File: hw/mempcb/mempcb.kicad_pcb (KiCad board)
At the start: 4 copper layers, 100 x 100 mm, 32 parts, among them J1 RC6502_Bus, J2 0.1" 2x25, U3 JEDEC_DIP32_RAM, U4 74LS138, U5 74LS138

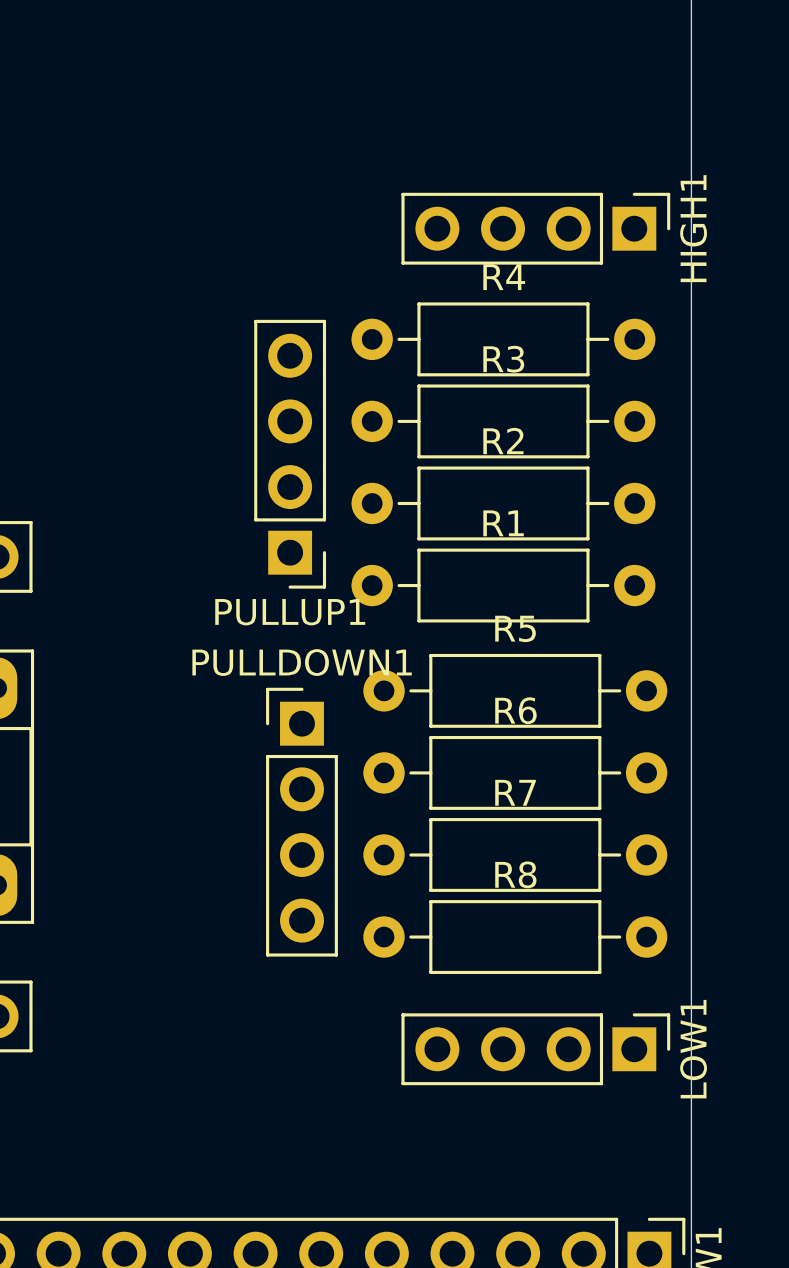
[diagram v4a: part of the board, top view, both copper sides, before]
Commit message: hw/mempcb/: Use just 4 pins instead of 8 for spare GND/Vcc
These don't need to be separate for each circuit, as the pullups do.
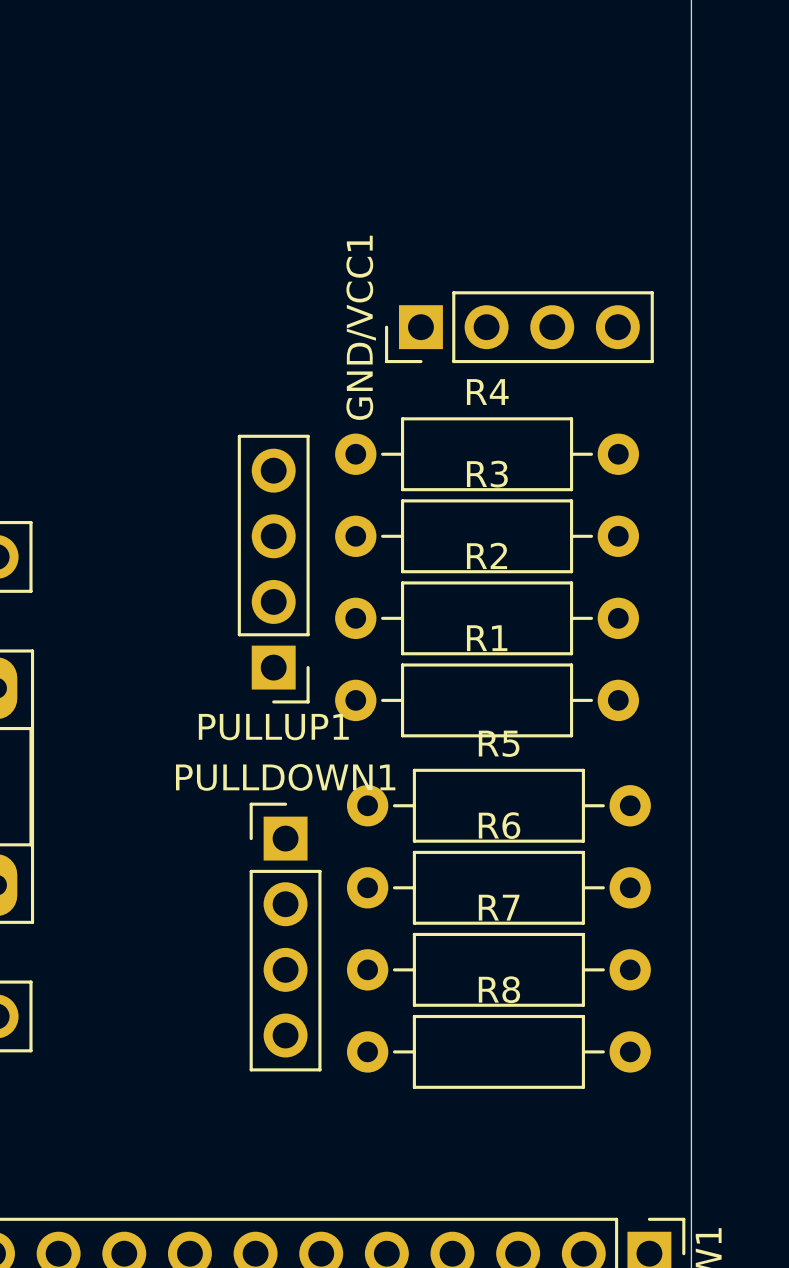
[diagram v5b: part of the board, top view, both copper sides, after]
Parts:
- removed LOW1: 0.1" 1x4, Connector_PinHeader_2.54mm:PinHeader_1x04_P2.54mm_Vertical
- moved GND/VCC1 9.09 mm to (169.5, 108.9), turned to 90 degrees
- moved R7 4.49 mm to (167.5, 133.8)
- moved R5 4.49 mm to (167.5, 127.4)
- moved R4 4.49 mm to (167.0, 113.8)
- moved R6 4.49 mm to (167.5, 130.6)
- moved R8 4.49 mm to (167.5, 137.0)
- moved PULLDOWN1 4.49 mm to (164.3, 128.7)
- moved PULLUP1 4.49 mm to (163.8, 122.1)
- moved R1 4.49 mm to (167.0, 123.4)
- moved R2 4.49 mm to (167.0, 120.2)
- moved R3 4.49 mm to (167.0, 117.0)
- renumbered HIGH1 to GND/VCC1
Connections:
- GND/VCC1 pad 1: /VCC -> /GND
- GND/VCC1 pad 2: /VCC -> /GND

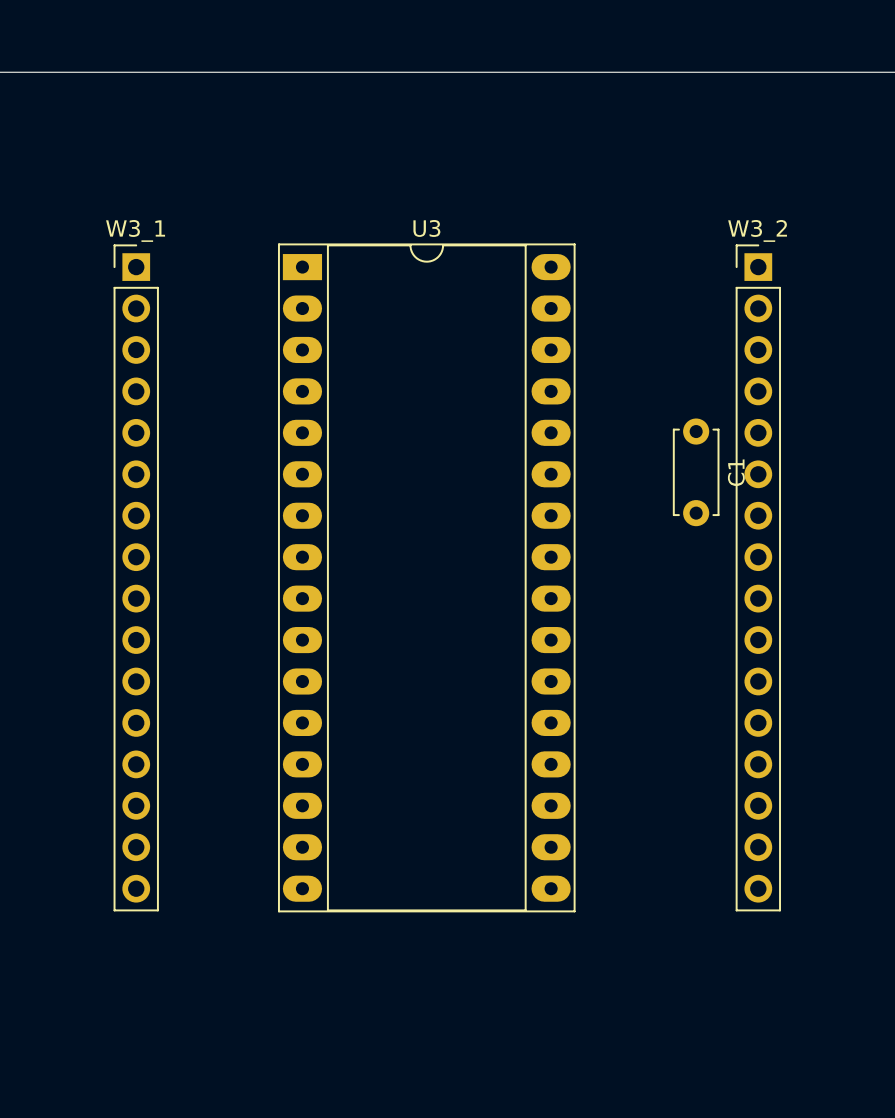
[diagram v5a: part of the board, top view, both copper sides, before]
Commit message: hw/mempcb/: Update ZIF socket footprint in layout
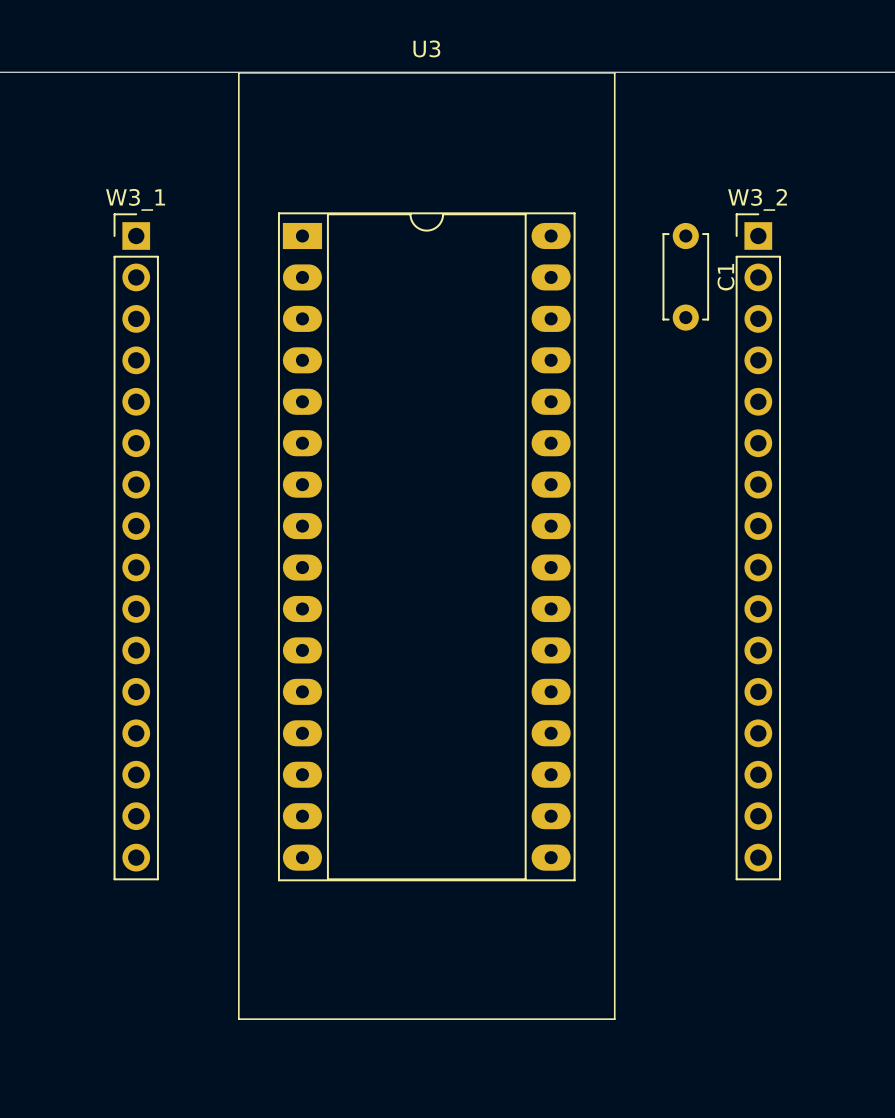
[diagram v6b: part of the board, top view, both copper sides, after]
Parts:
- U3: footprint Package_DIP:DIP-32_W15.24mm_Socket_LongPads -> mempcb:DIP-32_W15.24mm_ZIF_Socket_LongPads
- moved C1 12.0 mm to (140.3, 60.0)
- moved U3 1.91 mm to (116.8, 60.0)
- moved W3_1 1.91 mm to (106.6, 60.0)
- moved W3_2 1.91 mm to (144.8, 60.0)

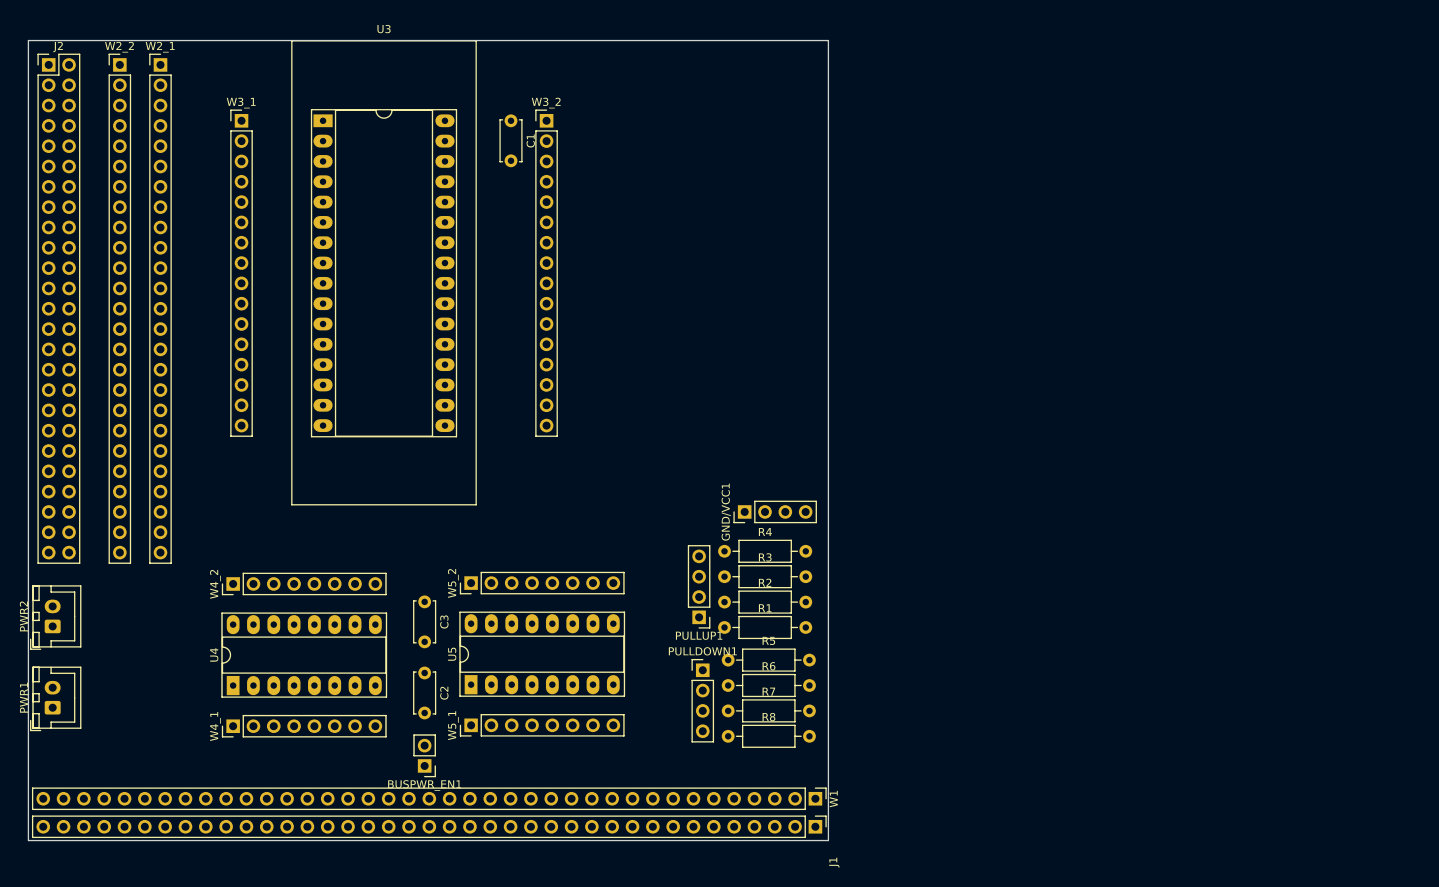
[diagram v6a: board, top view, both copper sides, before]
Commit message: hw/mempcb: Move all parts on to a .05"/1.27mm grid
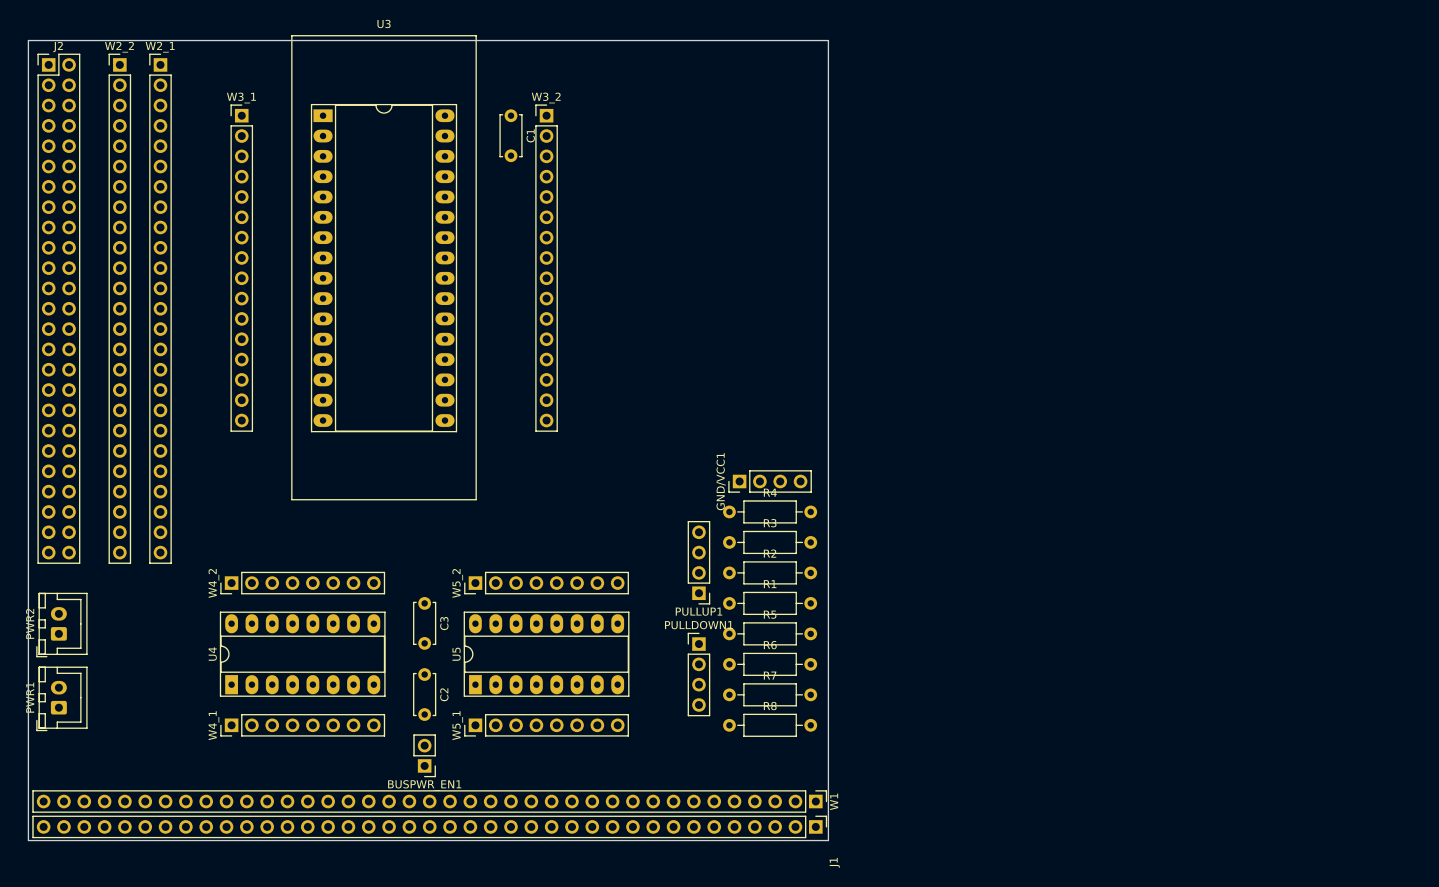
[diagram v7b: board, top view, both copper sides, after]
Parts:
- moved R4 4.96 mm to (167.6, 108.9)
- moved R3 4.33 mm to (167.6, 112.7)
- moved GND/VCC1 3.86 mm to (168.9, 105.1)
- moved R2 3.70 mm to (167.6, 116.5)
- moved PULLDOWN1 3.31 mm to (163.8, 125.4)
- moved R5 3.28 mm to (167.6, 124.2)
- moved R1 3.07 mm to (167.6, 120.4)
- moved PULLUP1 3.01 mm to (163.8, 119.1)
- moved R6 2.65 mm to (167.6, 128.0)
- moved R7 2.01 mm to (167.6, 131.8)
- moved R8 1.38 mm to (167.6, 135.6)
- moved PWR2 1.21 mm to (83.8, 124.2)
- moved PWR1 0.78 mm to (83.8, 133.4)
- moved W3_1 0.64 mm to (106.7, 59.4)
- moved C1 0.63 mm to (140.3, 59.4)
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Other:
- net class Default: clearance 0.127 -> 0.254; trace_width 0.127 -> 0.254; via_dia 0.6 -> 0.9; via_drill 0.3 -> 0.4
- net class Smallest added: clearance 0.127, trace_width 0.127, via_dia 0.6, via_drill 0.3
- rule trace_clearance: 0.127 -> 0.254
